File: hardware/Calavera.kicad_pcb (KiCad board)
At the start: 2 copper layers, 39.2 x 59.2 mm, 23 parts, among them Q1 DMN65D8L, SW1 SW_SPDT, U1 AT42QT1012, U2 LMV932

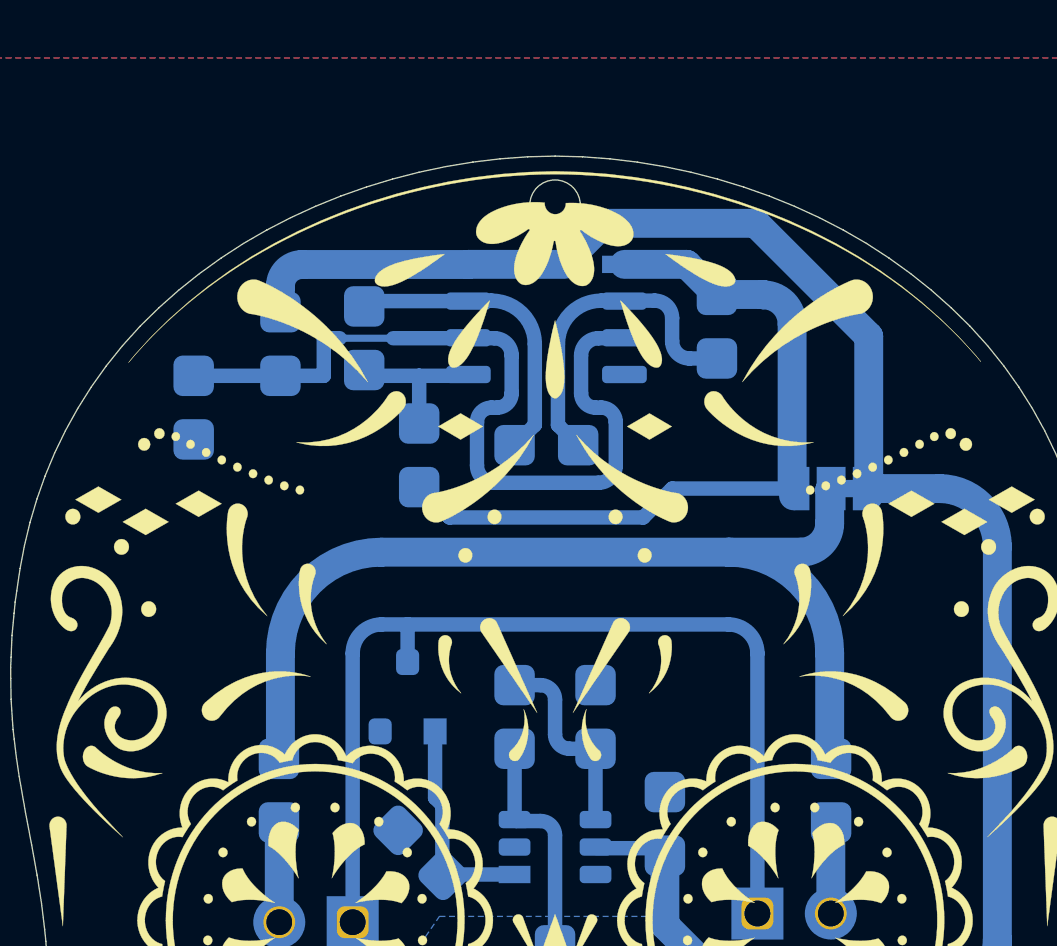
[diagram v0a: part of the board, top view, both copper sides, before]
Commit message: Simplified the values of the resistors * Added a new resistor * Moved tracks around * Added two vias to get GND to the bottom copper in an isolated island * Cleaned fabrication
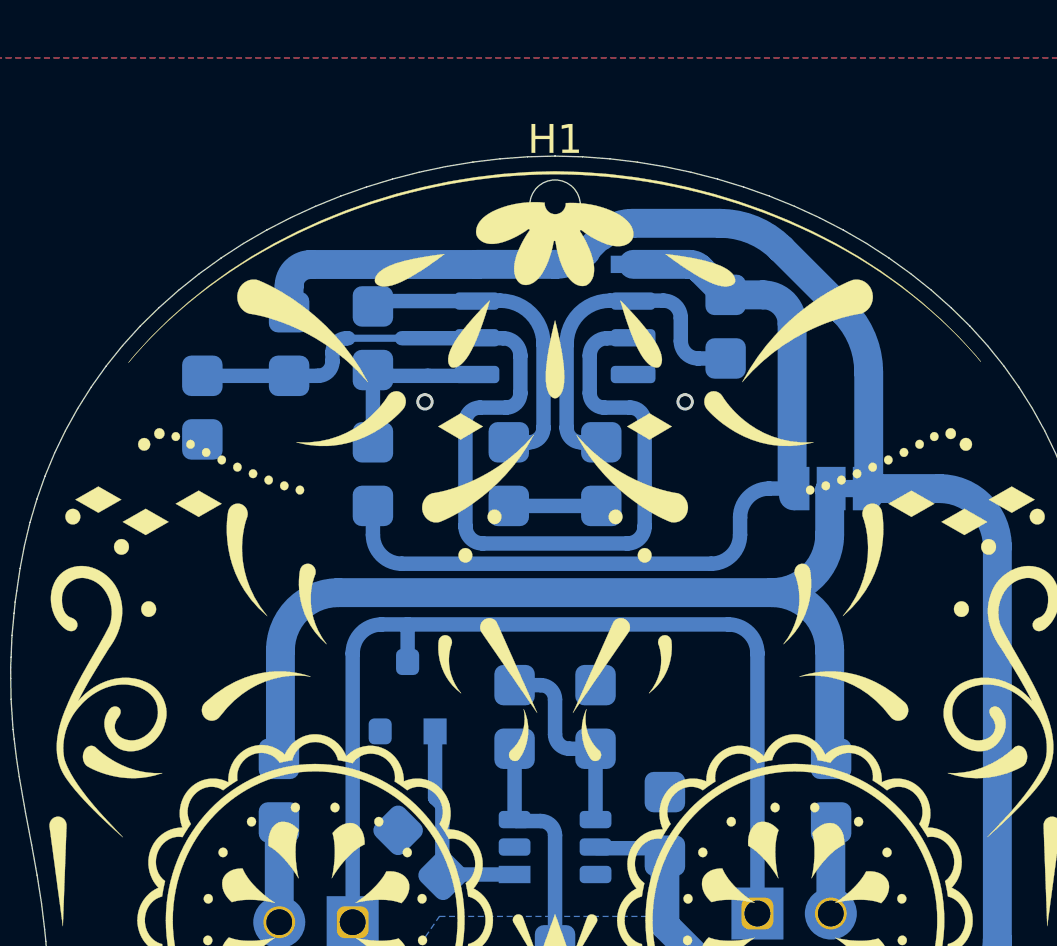
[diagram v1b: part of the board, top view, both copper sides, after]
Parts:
- added R4: 100kΩ, Calavera:0805-R_Handsolder, B.Cu at (98.4, 81.4)
- R5: renamed from R4; value 180kΩ -> 100kΩ
- R8: renamed from R7; value 1200Ω -> 1470Ω
- R9: renamed from R8; value 8200Ω -> 10kΩ
- moved R5 2.15 mm to (101.6, 81.4), turned to -90 degrees
- moved R8 1.73 mm to (93.7, 81.4)
- moved C3 0.30 mm to (105.9, 76.3)
- moved R10 0.30 mm to (90.8, 76.9)
- moved R11 0.30 mm to (87.8, 79.1)
- moved R9 0.30 mm to (93.7, 76.7)
- moved U2 0.30 mm to (100.0, 76.0)
- renumbered R9 to R10, R10 to R11, R5 to R6, R6 to R7
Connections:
- R5 pad 2: Net-(R4-Pad2) -> Net-(R4-Pad1)
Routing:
- net Vbias: track 29.0 -> 35.5 mm
- net Vfade: track 26.3 -> 29.9 mm
- net Net-(R4-Pad1): track 0.00 -> 3.20 mm
- net VLED: track 35.3 -> 33.3 mm
- net VJ1: track 5.35 -> 6.20 mm
- net VCC: track 78.2 -> 77.5 mm
- net Net-(U2A--): track 11.5 -> 12.1 mm
- net Net-(R4-Pad2): track 10.6 -> 11.1 mm
- net GND: vias 11 -> 13
